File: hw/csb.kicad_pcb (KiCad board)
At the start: 2 copper layers, 78 x 90 mm, 66 parts, among them J101 AMPSEAL_23_POS_VERT_BLUE_SEAL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, J102 AMPSEAL_8_POS_VERT_BLACK_SEAL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, J301 ARM_JTAG_SWD_HEADER_10_PINSMD, U301 LPC1549JBD64, U302 MCP2551_SOIC8, U401 VND5050AJTR-E, U501 VN5E010AH, U601 VN5E010AH, U701 VN5E010AH, U702 VN5E010AH, U901 VND5050AJTR-E, X301 XTAL_7A-12.000MAAJ-T

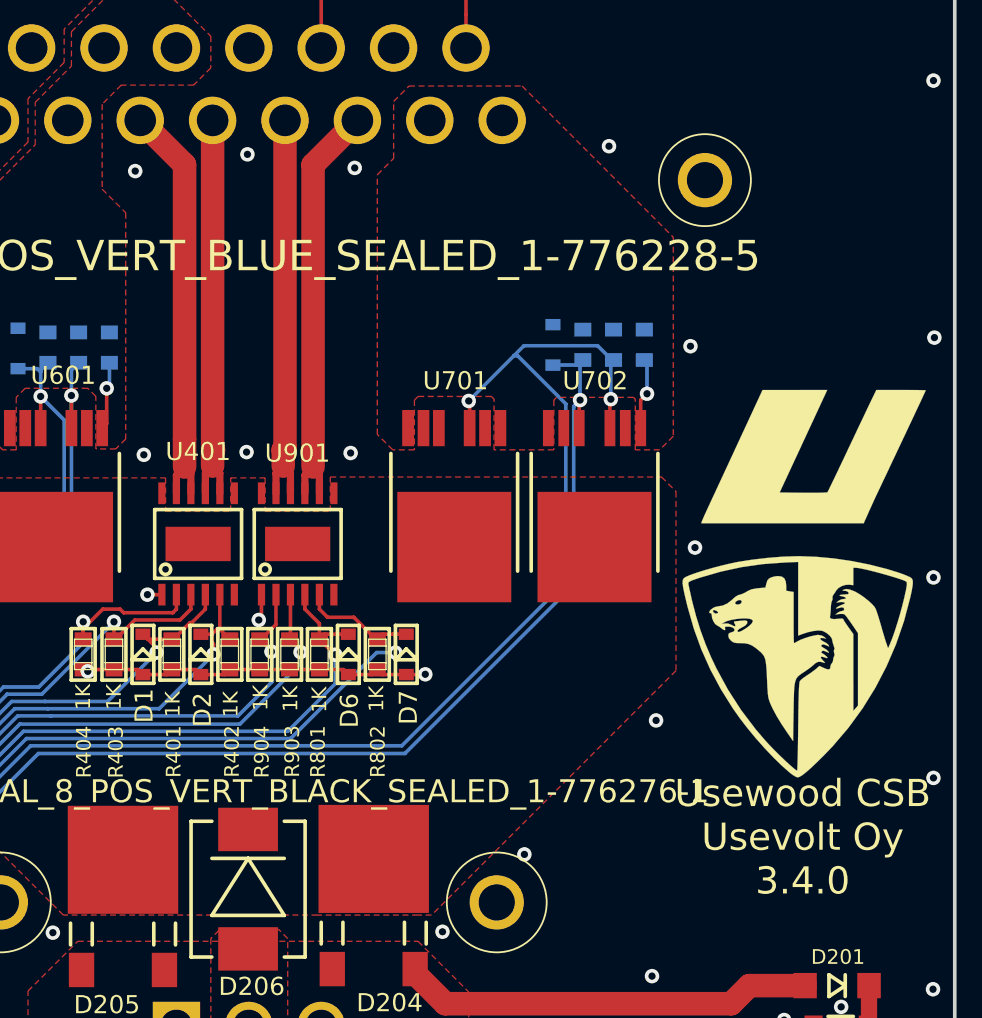
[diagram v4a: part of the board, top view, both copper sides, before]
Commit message: pcb 3.5.0 created, added protection diodes for vnd4040 outputs
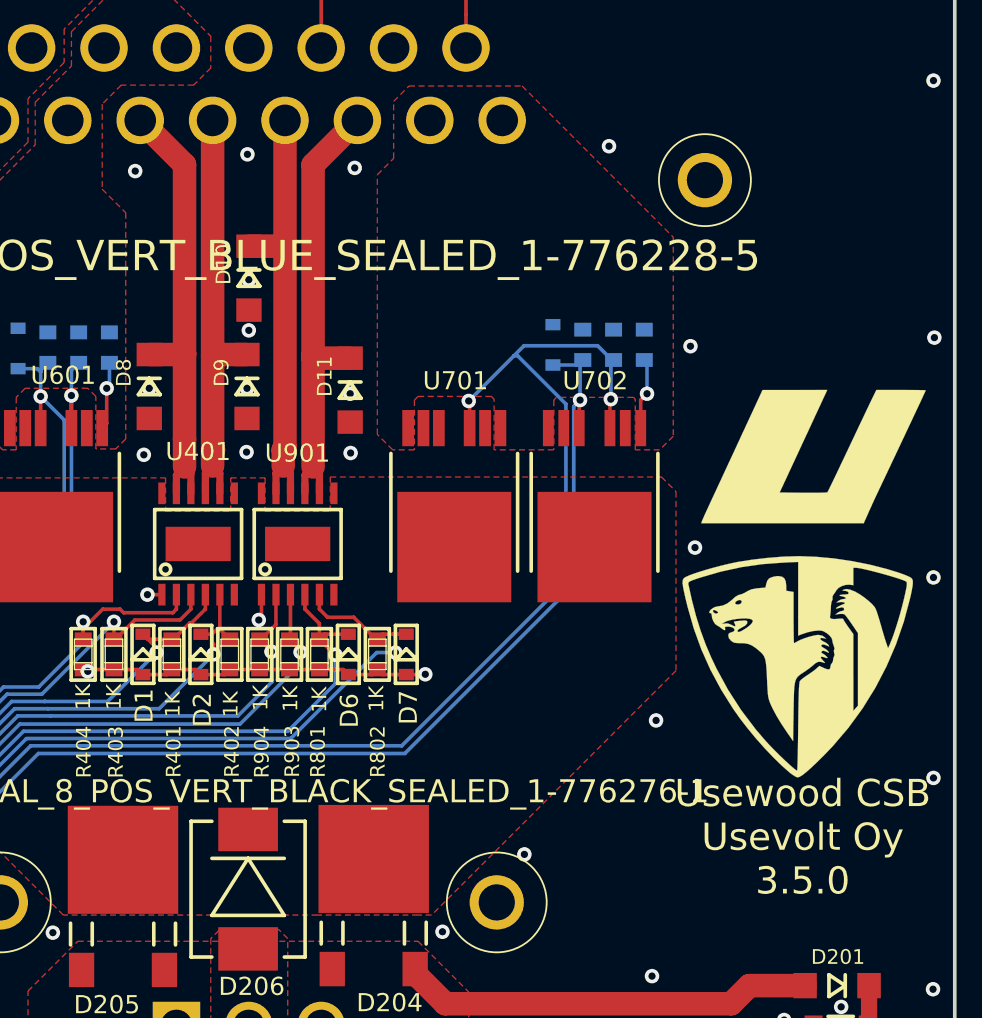
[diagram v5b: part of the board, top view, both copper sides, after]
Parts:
- added D10: DIODE_RS07J-GS18, usevolt:DO219AB, F.Cu at (168.0, 77.7)
- added D11: DIODE_RS07J-GS18, usevolt:DO219AB, F.Cu at (173.6, 83.9)
- added D8: DIODE_RS07J-GS18, usevolt:DO219AB, F.Cu at (162.5, 83.7)
- added D9: DIODE_RS07J-GS18, usevolt:DO219AB, F.Cu at (167.9, 83.7)
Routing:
- net /WIPER_4A: track 23.4 -> 25.6 mm
- net /IN_4A: track 22.5 -> 24.5 mm
- net /BEACON_4A: track 23.4 -> 25.4 mm
- net /BACK_4A: track 22.5 -> 24.4 mm
- net GND: vias 92 -> 97
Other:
- board text added: "Usewood CSB Usevolt Oy 3.5.0"
- board text removed: "Usewood CSB Usevolt Oy 3.4.0"
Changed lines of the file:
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@@
     (thickness 1.6)
     (drawings 9)
-    (tracks 677)
+    (tracks 695)
     (zones 0)
-    (modules 66)
+    (modules 70)
     (nets 89)
   )
@@
   )
   (setup
-    (last_trace_width 0.9)
+    (last_trace_width 1.3)
     (user_trace_width 0.3)
     (user_trace_width 0.5)
@@
     )
   )
+  (module usevolt:DO219AB (layer F.Cu)
+    (at 162.5 83.7 90)
+    (attr smd)
+    (fp_text reference D8 (at 0.762 -1.40462 90) (layer F.SilkS)
+      (effects (font (size 0.8128 0.8128) (thickness 0.0762)))
+    )
+    (fp_text value DIODE_RS07J-GS18 (at 0.19558 1.76784 90) (layer F.SilkS) hide
+      (effects (font (size 1.524 1.524) (thickness 0.15)))
+    )
+    (fp_line (start 0.44958 -0.59944) (end 0.44958 0.59944) (layer F.SilkS) (width 0.2032))
+    (fp_line (start 0.44958 0) (end -0.44958 -0.59944) (layer F.SilkS) (width 0.2032))
+    (fp_line (start -0.44958 0.59944) (end 0.44958 0) (layer F.SilkS) (width 0.2032))
+    (fp_line (start -0.44958 -0.59944) (end -0.44958 0.59944) (layer F.SilkS) (width 0.2032))
+    (pad P$2 smd rect (at 1.7653 0 90) (size 1.29794 1.39954) (layers F.Cu F.Paste F.Mask)
+      (net 15 /BEACON_4A))
+    (pad P$1 smd rect (at -1.7653 0 90) (size 1.29794 1.39954) (layers F.Cu F.Paste F.Mask)
+      (net 1 GND))
+    (model DO219AB.wrl
+      (at (xyz 0 0 0))
+      (scale (xyz 0.395 0.395 0.395))
+      (rotate (xyz 0 0 0))
+    )
+  )
+  (module usevolt:DO219AB (layer F.Cu)
+    (at 167.9 83.7 90)
+    (attr smd)
+    (fp_text reference D9 (at 0.762 -1.40462 90) (layer F.SilkS)
+      (effects (font (size 0.8128 0.8128) (thickness 0.0762)))
+    )
+    (fp_text value DIODE_RS07J-GS18 (at 0.19558 1.76784 90) (layer F.SilkS) hide
+      (effects (font (size 1.524 1.524) (thickness 0.15)))
+    )
+    (fp_line (start 0.44958 -0.59944) (end 0.44958 0.59944) (layer F.SilkS) (width 0.2032))
+    (fp_line (start 0.44958 0) (end -0.44958 -0.59944) (layer F.SilkS) (width 0.2032))
+    (fp_line (start -0.44958 0.59944) (end 0.44958 0) (layer F.SilkS) (width 0.2032))
+    (fp_line (start -0.44958 -0.59944) (end -0.44958 0.59944) (layer F.SilkS) (width 0.2032))
+    (pad P$2 smd rect (at 1.7653 0 90) (size 1.29794 1.39954) (layers F.Cu F.Paste F.Mask)
+      (net 16 /BACK_4A))
+    (pad P$1 smd rect (at -1.7653 0 90) (size 1.29794 1.39954) (layers F.Cu F.Paste F.Mask)
+      (net 1 GND))
+    (model DO219AB.wrl
+      (at (xyz 0 0 0))
+      (scale (xyz 0.395 0.395 0.395))
+      (rotate (xyz 0 0 0))
+    )
+  )
+  (module usevolt:DO219AB (layer F.Cu)
+    (at 168.008886 77.713152 90)
+    (attr smd)
+    (fp_text reference D10 (at 0.762 -1.40462 90) (layer F.SilkS)
+      (effects (font (size 0.8128 0.8128) (thickness 0.0762)))
+    )
+    (fp_text value DIODE_RS07J-GS18 (at 0.19558 1.76784 90) (layer F.SilkS) hide
+      (effects (font (size 1.524 1.524) (thickness 0.15)))
+    )
+    (fp_line (start -0.44958 -0.59944) (end -0.44958 0.59944) (layer F.SilkS) (width 0.2032))
+    (fp_line (start -0.44958 0.59944) (end 0.44958 0) (layer F.SilkS) (width 0.2032))
+    (fp_line (start 0.44958 0) (end -0.44958 -0.59944) (layer F.SilkS) (width 0.2032))
+    (fp_line (start 0.44958 -0.59944) (end 0.44958 0.59944) (layer F.SilkS) (width 0.2032))
+    (pad P$1 smd rect (at -1.7653 0 90) (size 1.29794 1.39954) (layers F.Cu F.Paste F.Mask)
+      (net 1 GND))
+    (pad P$2 smd rect (at 1.7653 0 90) (size 1.29794 1.39954) (layers F.Cu F.Paste F.Mask)
+      (net 17 /IN_4A))
+    (model DO219AB.wrl
+      (at (xyz 0 0 0))
+      (scale (xyz 0.395 0.395 0.395))
+      (rotate (xyz 0 0 0))
+    )
+  )
+  (module usevolt:DO219AB (layer F.Cu)
+    (at 173.6 83.9 90)
+    (attr smd)
+    (fp_text reference D11 (at 0.762 -1.40462 90) (layer F.SilkS)
+      (effects (font (size 0.8128 0.8128) (thickness 0.0762)))
+    )
+    (fp_text value DIODE_RS07J-GS18 (at 0.19558 1.76784 90) (layer F.SilkS) hide
+      (effects (font (size 1.524 1.524) (thickness 0.15)))
+    )
+    (fp_line (start -0.44958 -0.59944) (end -0.44958 0.59944) (layer F.SilkS) (width 0.2032))
+    (fp_line (start -0.44958 0.59944) (end 0.44958 0) (layer F.SilkS) (width 0.2032))
+    (fp_line (start 0.44958 0) (end -0.44958 -0.59944) (layer F.SilkS) (width 0.2032))
+    (fp_line (start 0.44958 -0.59944) (end 0.44958 0.59944) (layer F.SilkS) (width 0.2032))
+    (pad P$1 smd rect (at -1.7653 0 90) (size 1.29794 1.39954) (layers F.Cu F.Paste F.Mask)
+      (net 1 GND))
+    (pad P$2 smd rect (at 1.7653 0 90) (size 1.29794 1.39954) (layers F.Cu F.Paste F.Mask)
+      (net 18 /WIPER_4A))
+    (model DO219AB.wrl
+      (at (xyz 0 0 0))
+      (scale (xyz 0.395 0.395 0.395))
+      (rotate (xyz 0 0 0))
+    )
+  )
   (gr_line (start 129 137.000232) (end 129 51) (layer Edge.Cuts) (width 0.2))
   (gr_arc (start 205 51) (end 207 51) (angle -90) (layer Edge.Cuts) (width 0.2))
@@
   (gr_line (start 205 139) (end 131 139.000116) (layer Edge.Cuts) (width 0.2))
   (gr_arc (start 131 51) (end 131 49) (angle -90) (layer Edge.Cuts) (width 0.2))
-  (gr_text "Usewood CSB\nUsevolt Oy\n3.4.0\n" (at 198.6 108.6) (layer F.SilkS)
+  (gr_text "Usewood CSB\nUsevolt Oy\n3.5.0\n" (at 198.6 108.6) (layer F.SilkS)
     (effects (font (size 1.5 1.5) (thickness 0.3)))
   )
+  (via (at 173.6 84.1) (size 0.8) (drill 0.4) (layers F.Cu B.Cu) (net 1))
+  (via (at 168 77.8) (size 0.8) (drill 0.4) (layers F.Cu B.Cu) (net 1))
+  (via (at 168 80.6) (size 0.8) (drill 0.4) (layers F.Cu B.Cu) (net 1))
+  (via (at 167.9 83.8) (size 0.8) (drill 0.4) (layers F.Cu B.Cu) (net 1))
+  (via (at 162.5 83.8) (size 0.8) (drill 0.4) (layers F.Cu B.Cu) (net 1))
   (via (at 196 125.9) (size 0.8) (drill 0.4) (layers F.Cu B.Cu) (net 1))
   (via (at 191.7 137.6) (size 0.8) (drill 0.4) (layers F.Cu B.Cu) (net 1))
@@
   (segment (start 160.3 82.3882) (end 160.3 83.65) (width 0.2) (layer B.Cu) (net 14))
   (via (at 160.15 83.8) (size 0.8) (drill 0.4) (layers F.Cu B.Cu) (net 14))
+  (segment (start 164.45 81.9) (end 164.45 71.44744) (width 1.3) (layer F.Cu) (net 15))
+  (segment (start 164.45 86.6) (end 164.45 81.9) (width 1.3) (layer F.Cu) (net 15))
+  (segment (start 162.5 81.9347) (end 164.4153 81.9347) (width 1.3) (layer F.Cu) (net 15))
+  (segment (start 164.4153 81.9347) (end 164.45 81.9) (width 1.3) (layer F.Cu) (net 15))
   (segment (start 164.45 86.6) (end 164.45 88.15) (width 1.3) (layer F.Cu) (net 15))
-  (segment (start 164.45 86.6) (end 164.45 71.44744) (width 1.3) (layer F.Cu) (net 15))
   (segment (start 164.45 71.44744) (end 162.00052 68.99796) (width 1.3) (layer F.Cu) (net 15))
   (segment (start 164.45 88.15) (end 164.8 88.5) (width 0.4) (layer F.Cu) (net 15))
@@
   (segment (start 164 89.6) (end 164 88.6) (width 0.4) (layer F.Cu) (net 15))
   (segment (start 164 88.6) (end 164.45 88.15) (width 0.4) (layer F.Cu) (net 15))
+  (segment (start 166.00102 82) (end 166.00102 68.99796) (width 1.3) (layer F.Cu) (net 16))
+  (segment (start 166.00102 87.15102) (end 166.00102 82) (width 1.3) (layer F.Cu) (net 16))
+  (segment (start 167.9 81.9347) (end 166.06632 81.9347) (width 1.3) (layer F.Cu) (net 16))
+  (segment (start 166.06632 81.9347) (end 166.00102 82) (width 1.3) (layer F.Cu) (net 16))
   (segment (start 166 87.25) (end 166 88.1) (width 1.3) (layer F.Cu) (net 16))
   (segment (start 166.05 87.2) (end 166.00102 87.15102) (width 1.3) (layer F.Cu) (net 16))
-  (segment (start 166.00102 87.15102) (end 166.00102 68.99796) (width 1.3) (layer F.Cu) (net 16))
   (segment (start 166 87.25) (end 166.05 87.2) (width 1.3) (layer F.Cu) (net 16))
   (segment (start 166 88.1) (end 166.4 88.5) (width 0.4) (layer F.Cu) (net 16))
@@
   (segment (start 165.6 88.5) (end 166 88.1) (width 0.4) (layer F.Cu) (net 16))
   (segment (start 165.6 89.6) (end 165.6 88.5) (width 0.4) (layer F.Cu) (net 16))
+  (segment (start 169.99898 76) (end 169.99898 68.99796) (width 1.3) (layer F.Cu) (net 17))
+  (segment (start 169.99898 87.10102) (end 169.99898 76) (width 1.3) (layer F.Cu) (net 17))
+  (segment (start 168.008886 75.947852) (end 169.946832 75.947852) (width 1.3) (layer F.Cu) (net 17))
+  (segment (start 169.946832 75.947852) (end 169.99898 76) (width 1.3) (layer F.Cu) (net 17))
   (segment (start 169.9 87.2) (end 169.9 88.1) (width 1.3) (layer F.Cu) (net 17))
   (segment (start 169.9 87.2) (end 169.99898 87.10102) (width 1.3) (layer F.Cu) (net 17))
-  (segment (start 169.99898 87.10102) (end 169.99898 68.99796) (width 1.3) (layer F.Cu) (net 17))
   (segment (start 169.9 88.1) (end 170.3 88.5) (width 0.4) (layer F.Cu) (net 17))
   (segment (start 170.3 88.5) (end 170.3 89.6) (width 0.4) (layer F.Cu) (net 17))
   (segment (start 169.5 88.5) (end 169.9 88.1) (width 0.4) (layer F.Cu) (net 17))
   (segment (start 169.5 89.6) (end 169.5 88.5) (width 0.4) (layer F.Cu) (net 17))
-  (segment (start 171.55 88.15) (end 171.55 71.44744) (width 1.3) (layer F.Cu) (net 18))
+  (segment (start 171.55 82) (end 171.55 71.44744) (width 1.3) (layer F.Cu) (net 18))
+  (segment (start 171.55 88.15) (end 171.55 82) (width 1.3) (layer F.Cu) (net 18))
+  (segment (start 173.6 82.1347) (end 171.60023 82.1347) (width 1.3) (layer F.Cu) (net 18))
+  (segment (start 171.60023 82.1347) (end 171.55 82.08447) (width 1.3) (layer F.Cu) (net 18))
+  (segment (start 171.55 82.08447) (end 171.55 82) (width 1.3) (layer F.Cu) (net 18))
   (segment (start 171.55 71.44744) (end 173.99948 68.99796) (width 1.3) (layer F.Cu) (net 18))
   (segment (start 171.55 88.15) (end 171.9 88.5) (width 0.4) (layer F.Cu) (net 18))

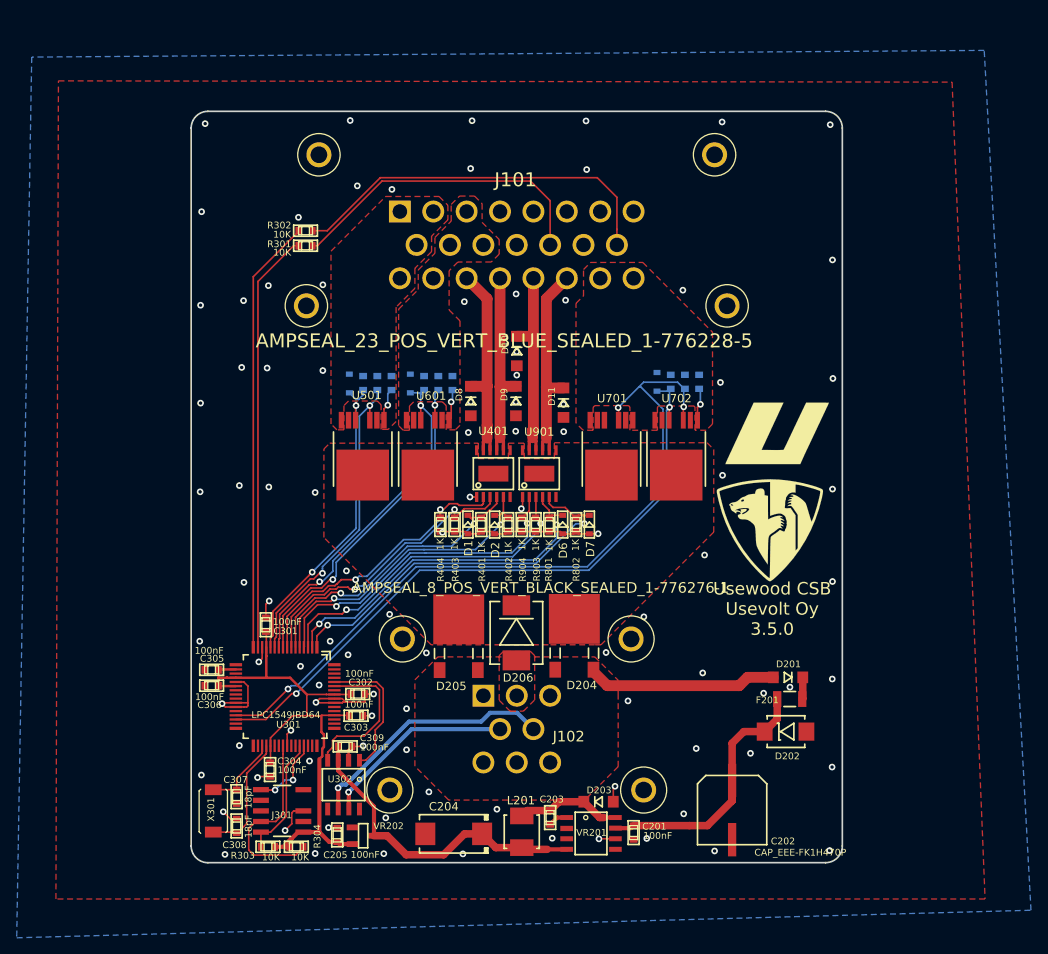
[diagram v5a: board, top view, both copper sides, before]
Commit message: silkscreen updated for 3.5.0
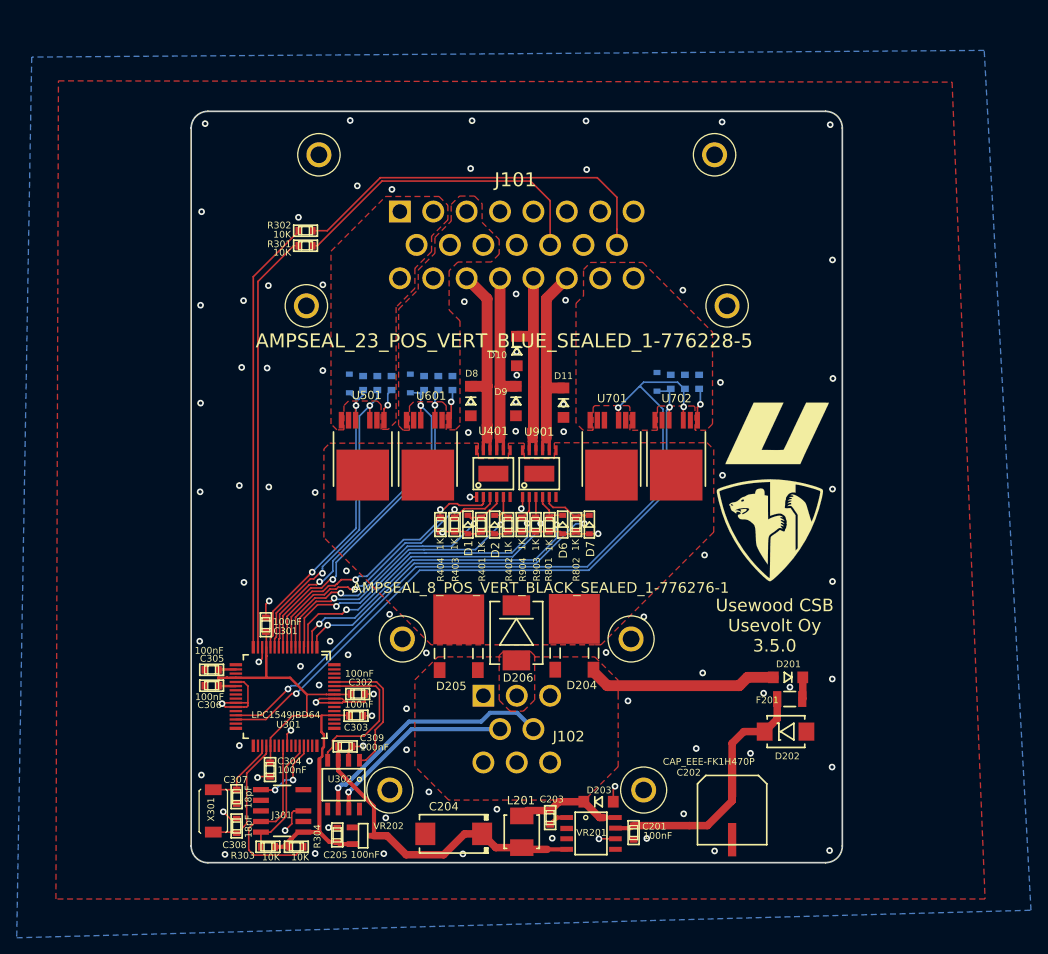
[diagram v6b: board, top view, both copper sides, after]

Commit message: pcb 3.6.0 created, with double fets in work & drive lights
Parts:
- removed R501, R502, R601, R602, R701, R702: 1K, yageo:0603
- removed U501, U601, U701, U702: VN5E010AH, usevolt:HPAK
- added R4: 1K, yageo:0603, F.Cu at (149.8, 82.7)
- added R5: 1K, yageo:0603, F.Cu at (149.5, 81.1)
- added R6: 10K, yageo:0603, F.Cu at (149.6, 78.0)
- added R7: 1K, yageo:0603, F.Cu at (187.2, 83.0)
- added R8: 1K, yageo:0603, F.Cu at (186.9, 81.5)
- added R9: 10K, yageo:0603, F.Cu at (187.0, 78.3)
- added U1: VN5E010AH, usevolt:HPAK, F.Cu at (133.8, 92.5)
- added U2: VN5E010AH, usevolt:HPAK, F.Cu at (141.7, 92.5)
- added U3: VN5E010AH, usevolt:HPAK, F.Cu at (157.3, 92.5)
- added U4: VN5E010AH, usevolt:HPAK, F.Cu at (149.6, 92.5)
- added U5: VN5E010AH, usevolt:HPAK, F.Cu at (179.3, 92.4)
- added U6: VN5E010AH, usevolt:HPAK, F.Cu at (187.1, 92.5)
- D3, D4, D5, R3: moved to F.Cu
- R1, R2: value 10K -> 1K; moved to F.Cu
- moved R3 48.2 mm to (141.8, 78.0), turned to 180 degrees
- moved R2 18.7 mm to (141.7, 81.0), turned to 0 degrees
- moved R1 11.2 mm to (141.8, 82.7), turned to 0 degrees
- moved R301 7.06 mm to (137.1, 60.8)
- moved R302 7.06 mm to (137.1, 59.0)
- moved D3 6.59 mm to (141.7, 79.5), turned to 0 degrees
- moved D4 6.10 mm to (149.5, 79.5), turned to 0 degrees
- moved D5 2.66 mm to (187.0, 79.9), turned to 0 degrees
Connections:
- R1 pad 2: /DRIVE_15A -> /LPC1549/DRIVE
- R2 pad 1: GND -> /LPC1549/DRIVE_SENSE
- R2 pad 2: /WORK_15A -> GND
- R3 pad 2: /COOLER_30A -> /DRIVE_15A
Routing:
- net GND: track 67.5 -> 84.3 mm, vias 97 -> 100
- net Net-(R301-Pad2): track 50.5 -> 58.8 mm, vias 0 -> 2
- net Net-(R302-Pad2): track 52.1 -> 60.1 mm, vias 0 -> 2
- net /LPC1549/DRIVE: track 38.1 -> 45.1 mm, vias 2 -> 3
- net /Sheet5A019745/IN1: track 41.3 -> 47.2 mm, vias 2 -> 3
- net /LPC1549/COOLER: track 91.0 -> 85.9 mm
- net /LPC1549/COOLER_P: track 45.8 -> 50.2 mm
- net /LPC1549/WIPER_POS: track 37.9 -> 42.3 mm
- net /DRIVE_15A: track 3.98 -> 0.00 mm, vias 1 -> 0
- net /COOLER_30A: track 3.97 -> 0.00 mm, vias 1 -> 0
- net /WORK_15A: track 3.78 -> 0.00 mm, vias 1 -> 0
- net /Sheet5A019745/SENSE1: track 42.9 -> 40.4 mm
- net /LPC1549/DRIVE_SENSE: track 38.5 -> 37.1 mm
- net /LPC1549/COOLER_SENSE: track 78.8 -> 80.0 mm
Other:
- board text added: "Usewood CSB Usevolt Oy 3.6.0"
- board text removed: "Usewood CSB Usevolt Oy 3.5.0"
